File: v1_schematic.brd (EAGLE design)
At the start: 150.8 x 88.9 mm, 212 parts, among them IC1 PCA82C250, IC2 FT232RL, IC3 SP3223EBP, IC4 MAX481CPA, IC5 LM2576T, Q1 25MHz, Q2 32.768kHz, Q3 2N2222A, T1 ST02-3.5MM, T3 2N2222, T4 2N2222, T5 2N2222, T6 2N2222, T7 2N2222, U1 ON_SEMICONDUCTOR_NCP1117ST33T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, U2 ON_SEMICONDUCTOR_NCP1117ST50T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, X1 MINI-USB-32005-201, X10 PC817SW, X11 PC817SW, X12 PC817SW, X13 PC817SW, X14 PC817SW, X15 PC817SW, X16 PC817SW, X17 PC817SW, X18 PC817SW, X19 PC817SW, X20 PC817SW, X21 PC817SW, X22 PC817SW, X23 PC817SW, X24 PC817SW, X7 5566-8, X8 5566-8, X9 PC817SW

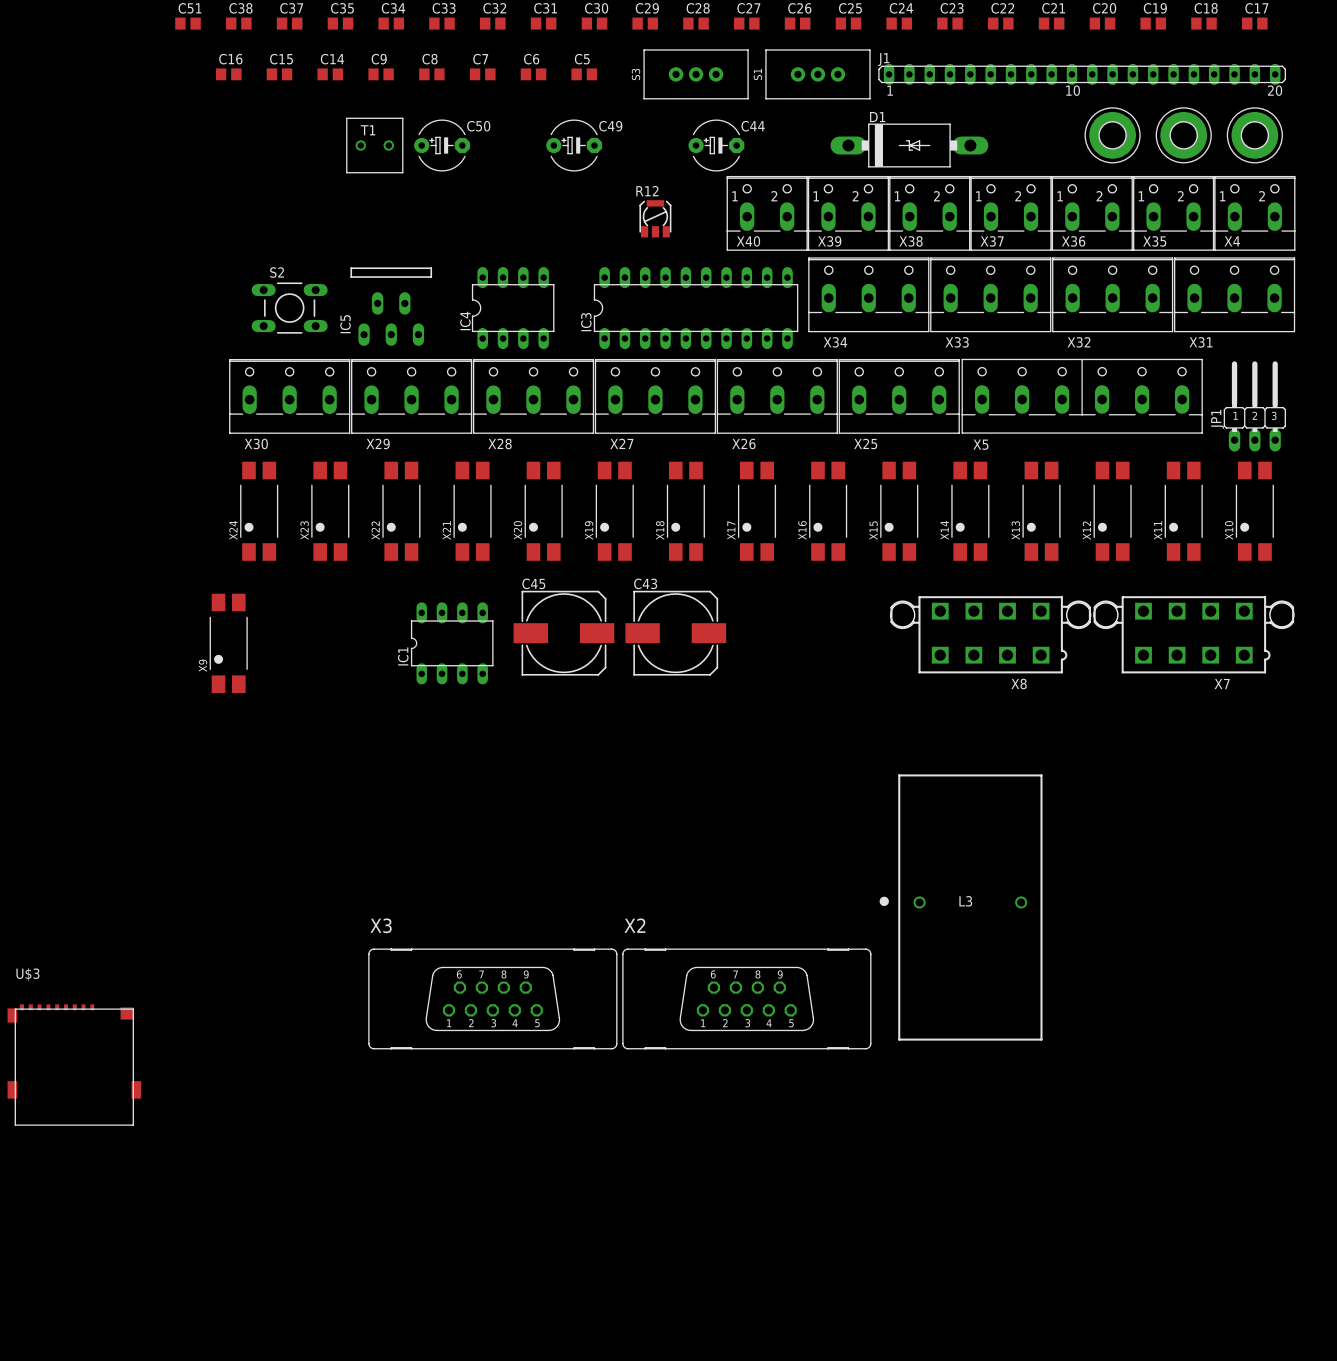
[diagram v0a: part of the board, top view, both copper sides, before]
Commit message: JTAG connector
- Changed JTAG connector to dual row
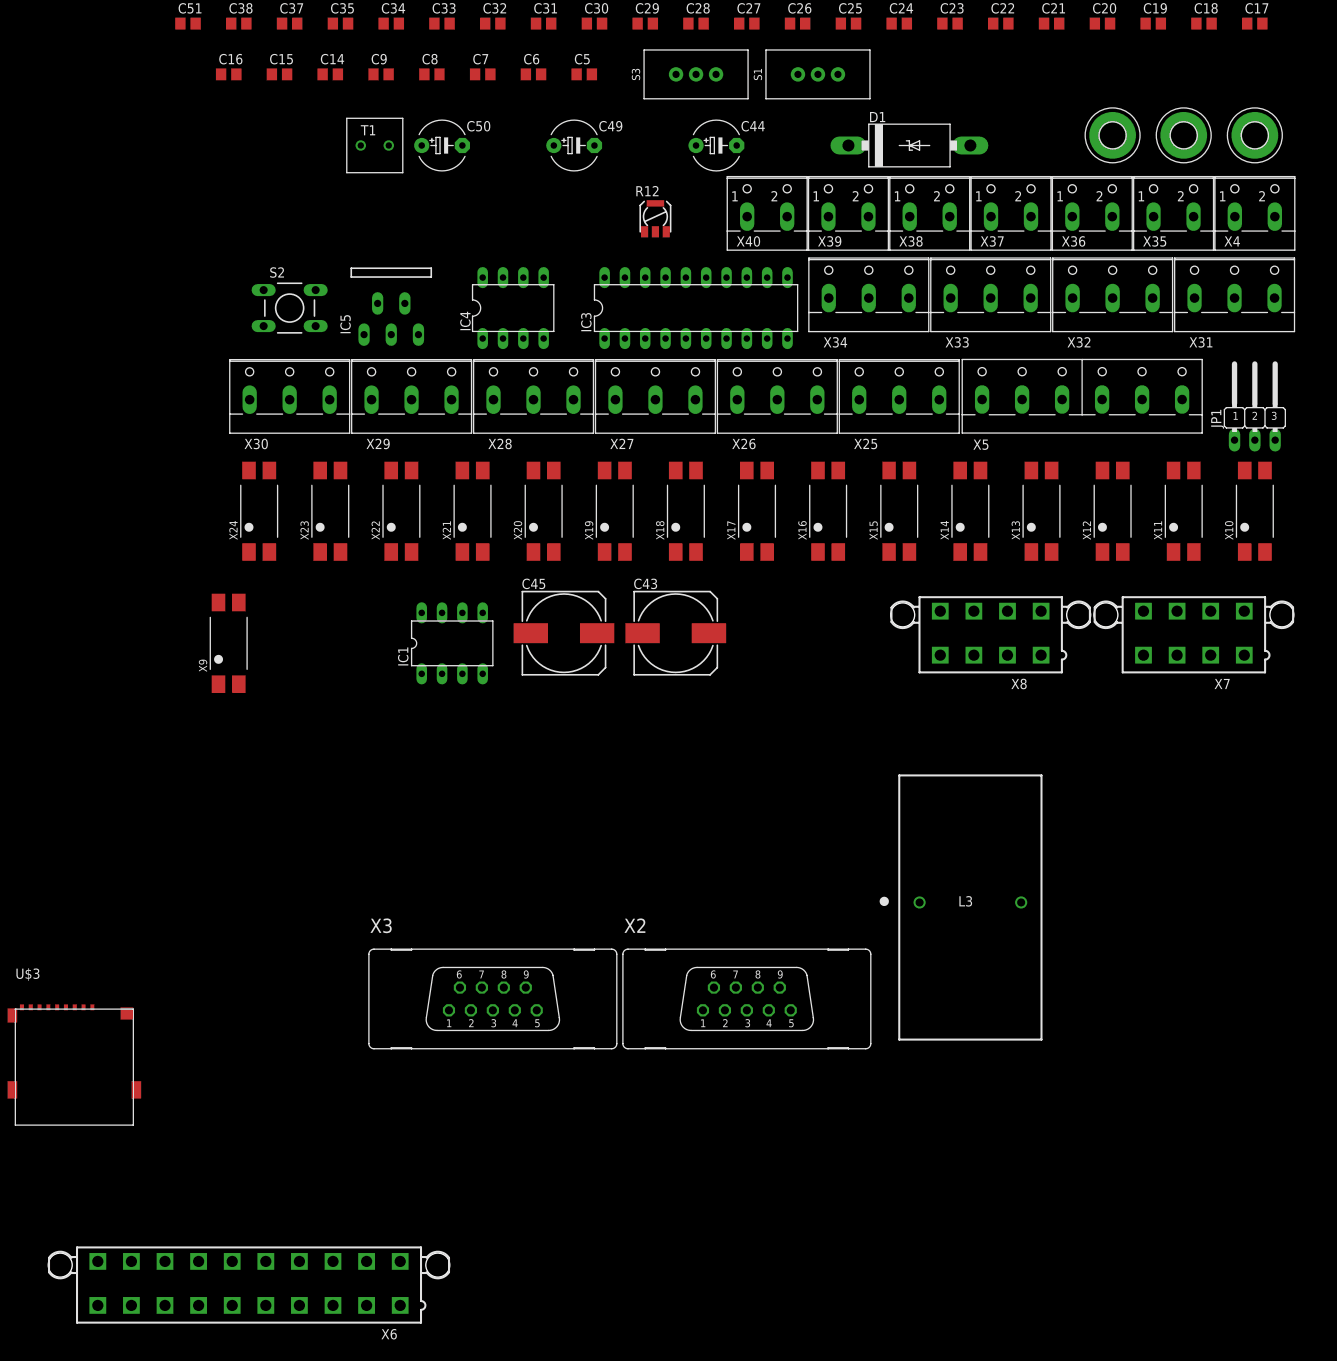
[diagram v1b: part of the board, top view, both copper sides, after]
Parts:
- removed J1: (no value), con-lsta:JBK20
- added X6: 5566-20, con-molex:5566-20
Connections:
- net +3V3: now also X6.1, X6.2; no longer J1.1, J1.2
- net GND: now also X6.10, X6.12, X6.14, X6.16, X6.18, X6.20, X6.4, X6.6, X6.8; no longer J1.10, J1.12, J1.14, J1.16, J1.18, J1.20, J1.4, J1.6, J1.8
- net N$50: now also X6.11; no longer J1.11
- net N$53: now also X6.17; no longer J1.17
- net N$56: now also X6.19; no longer J1.19
- net NRF_SCK: now also X6.13; no longer J1.13
- net RESET#: now also X6.15; no longer J1.15
- net TCK/SWCLK: now also X6.9; no longer J1.9
- net TDI: now also X6.5; no longer J1.5
- net TMS/SWDIO: now also X6.7; no longer J1.7
- net TRST: now also X6.3; no longer J1.3

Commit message: Minor Board Edits
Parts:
- moved DIR1 394.9 mm to (39.4, -203.8)
- moved DIR7 394.9 mm to (-6.32, -203.8)
- moved DIR10 394.9 mm to (-29.2, -203.8)
- moved DIR11 394.9 mm to (-36.8, -203.8)
- moved DIR2 394.9 mm to (31.8, -203.8)
- moved DIR3 394.9 mm to (24.2, -203.8)
- moved DIR4 394.9 mm to (16.5, -203.8)
- moved DIR5 394.9 mm to (8.92, -203.8)
- moved DIR6 394.9 mm to (1.30, -203.8)
- moved DIR8 394.9 mm to (-13.9, -203.8)
- moved DIR9 394.9 mm to (-21.6, -203.8)
- moved NPN1 364.6 mm to (62.2, -159.7)
- moved NPN8 364.6 mm to (8.82, -159.7)
- moved NPN10 364.6 mm to (-6.42, -159.7)
- moved NPN2 364.6 mm to (54.5, -159.7)
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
